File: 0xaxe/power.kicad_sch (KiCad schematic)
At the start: 24 parts, among them Q1 BSS138, Q2 TPH1R712MD,L1Q, Q3 TPH1R712MD,L1Q, Q5 TPH1R712MD,L1Q, U2 1117-3.3, U2 74LVC1G175, U3 AP3211

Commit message: rev1.2
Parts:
- added C218, C225: 1µ, Capacitor_SMD:C_0805_2012Metric, symbol Device:C
- added U113: NCP718xSN500, Package_TO_SOT_SMD:SOT-23-5, symbol Regulator_Linear:NCP718xSN500
- R24: value 84.5k -> 49.9k; Distributor (none) -> D; Manufacturer (none) -> RC0805FR-0749K9L; OrderNr (none) -> 311-49.9KCRCT-ND
- R25: value 16.3k -> 7.15k; Distributor (none) -> D; Manufacturer (none) -> RMCF0805FT7K15; OrderNr (none) -> RMCF0805FT7K15CT-ND
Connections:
- net +5V: now also C218.1, U113.5 (OUT); no longer C9.1, JP1.2 (B), U2.3 (VI)
- net GND: now also C218.2, C225.2, U113.2 (GND)
- new net +6.5V: C225.1, C9.1, JP1.2 (B), U113.1 (IN), U113.3 (EN), U2.3 (VI)
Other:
- moved on the sheet: C15, C2, C24, C4, C9, D9, JP1, JP2, L1, Q1, Q2, Q3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

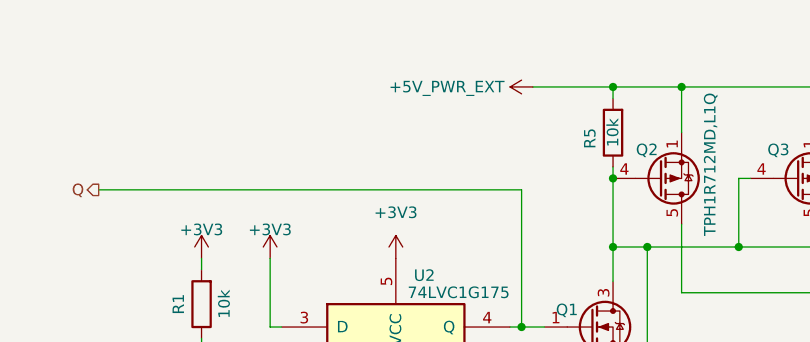
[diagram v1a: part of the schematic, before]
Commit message: Add F2 Fuse for 5V external supply
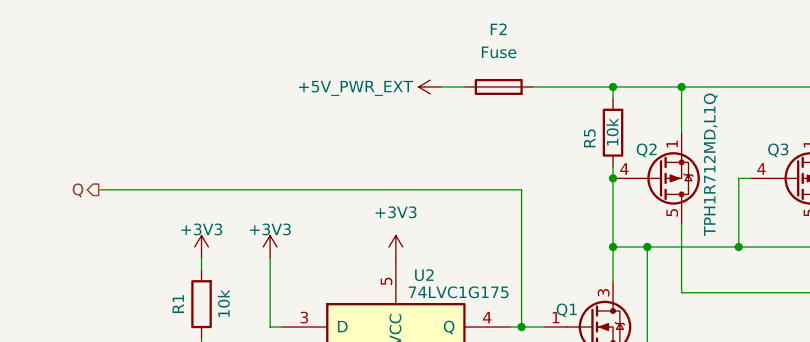
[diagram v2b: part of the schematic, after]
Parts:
- added F2: Fuse, Fuse:Fuseholder_Blade_Mini_Keystone_3568, symbol Device:Fuse
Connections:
- net +5V_PWR_EXT: now also F2.1; no longer Q2.1 (S), Q2.2 (S), Q2.3 (S), Q3.1 (S), Q3.2 (S), Q3.3 (S), Q5.1 (S), Q5.2 (S), Q5.3 (S), R5.2
- new net: F2.2, Q2.1 (S), Q2.2 (S), Q2.3 (S), Q3.1 (S), Q3.2 (S), Q3.3 (S), Q5.1 (S), Q5.2 (S), Q5.3 (S), R5.2
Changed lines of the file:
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@@
 	(wire
 		(pts
+			(xy 124.46 21.59) (xy 127 21.59)
+		)
+		(stroke
+			(width 0)
+			(type default)
+		)
+	)
+	(wire
+		(pts
 			(xy 176.53 115.57) (xy 176.53 127)
 		)
@@
 	)
 	(symbol
+		(lib_id "Device:Fuse")
+		(at 130.81 21.59 90)
+		(unit 1)
+		(exclude_from_sim no)
+		(in_bom yes)
+		(on_board yes)
+		(dnp no)
+		(fields_autoplaced yes)
+		(property "Reference" "F2"
+			(at 130.81 15.24 90)
+			(effects
+				(font
+					(size 1.27 1.27)
+				)
+			)
+		)
+		(property "Value" "Fuse"
+			(at 130.81 17.78 90)
+			(effects
+				(font
+					(size 1.27 1.27)
+				)
+			)
+		)
+		(property "Footprint" "Fuse:Fuseholder_Blade_Mini_Keystone_3568"
+			(at 130.81 23.368 90)
+			(effects
+				(font
+					(size 1.27 1.27)
+				)
+				(hide yes)
+			)
+		)
+		(property "Datasheet" "~"
+			(at 130.81 21.59 0)
+			(effects
+				(font
+					(size 1.27 1.27)
+				)
+				(hide yes)
+			)
+		)
+		(property "Description" "Fuse"
+			(at 130.81 21.59 0)
+			(effects
+				(font
+					(size 1.27 1.27)
+				)
+				(hide yes)
+			)
+		)
+		(pin "1"
+		)
+		(pin "2"
+		)
+		(instances
+			(project "0xaxe"
+				(path "/e63e39d7-6ac0-4ffd-8aa3-1841a4541b55/8ec0a9c6-2b78-44ef-a83d-9047d2828409"
+					(reference "F2")
+					(unit 1)
+				)
+			)
+		)
+	)
+	(symbol
 		(lib_id "74xGxx:74LVC1G175")
 		(at 119.38 53.34 0)
@@
 	(symbol
 		(lib_id "mylib7:+5V_PWR_EXT")
-		(at 134.62 21.59 90)
+		(at 124.46 21.59 90)
 		(unit 1)
 		(exclude_from_sim no)
@@
 		(on_board yes)
 		(dnp no)
-		(fields_autoplaced yes)
 		(property "Reference" "#PWR030"
-			(at 138.43 21.59 0)
+			(at 128.27 21.59 0)
 			(effects
 				(font
@@
 		)
 		(property "Value" "+5V_PWR_EXT"
-			(at 131.445 21.59 90)
+			(at 121.285 21.59 90)
 			(effects
 				(font
@@
 		)
 		(property "Footprint" ""
-			(at 134.62 21.59 0)
+			(at 124.46 21.59 0)
 			(effects
 				(font
@@
 		)
 		(property "Datasheet" ""
-			(at 134.62 21.59 0)
+			(at 124.46 21.59 0)
 			(effects
 				(font
@@
 		)
 		(property "Description" ""
-			(at 134.62 21.59 0)
+			(at 124.46 21.59 0)
 			(effects
 				(font

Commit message: General Update
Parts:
- removed F2: Fuse, Fuse:Fuseholder_Blade_Mini_Keystone_3568, symbol Device:Fuse
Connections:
- net +5V_PWR_EXT: now also Q2.1 (S), Q2.2 (S), Q2.3 (S), Q3.1 (S), Q3.2 (S), Q3.3 (S), Q5.1 (S), Q5.2 (S), Q5.3 (S), R5.2
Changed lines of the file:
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@@
-	(wire
-		(pts
-			(xy 143.51 21.59) (xy 134.62 21.59)
-		)
-		(stroke
-			(width 0)
-			(type default)
-		)
-	)
 	(wire
 		(pts
@@
 	(wire
 		(pts
-			(xy 124.46 21.59) (xy 127 21.59)
+			(xy 124.46 21.59) (xy 143.51 21.59)
 		)
 		(stroke
@@
 					(unit 1)
 				)
-			)
-		)
-	)
-	(symbol
-		(lib_id "Device:Fuse")
-		(at 130.81 21.59 90)
-		(unit 1)
-		(exclude_from_sim no)
-		(in_bom yes)
-		(on_board yes)
-		(dnp no)
-		(fields_autoplaced yes)
-		(property "Reference" "F2"
-			(at 130.81 15.24 90)
-			(effects
-				(font
-					(size 1.27 1.27)
-				)
-			)
-		)
-		(property "Value" "Fuse"
-			(at 130.81 17.78 90)
-			(effects
-				(font
-					(size 1.27 1.27)
-				)
-			)
-		)
-		(property "Footprint" "Fuse:Fuseholder_Blade_Mini_Keystone_3568"
-			(at 130.81 23.368 90)
-			(effects
-				(font
-					(size 1.27 1.27)
-				)
-				(hide yes)
-			)
-		)
-		(property "Datasheet" "~"
-			(at 130.81 21.59 0)
-			(effects
-				(font
-					(size 1.27 1.27)
-				)
-				(hide yes)
-			)
-		)
-		(property "Description" "Fuse"
-			(at 130.81 21.59 0)
-			(effects
-				(font
-					(size 1.27 1.27)
-				)
-				(hide yes)
-			)
-		)
-		(pin "1"
-		)
-		(pin "2"
-		)
-		(instances
-			(project "0xaxe"
-				(path "/e63e39d7-6ac0-4ffd-8aa3-1841a4541b55/8ec0a9c6-2b78-44ef-a83d-9047d2828409"
-					(reference "F2")
-					(unit 1)
-				)

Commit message: fixed couple of things
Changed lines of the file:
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@@
 		)
 		(property "Value" "GND"
-			(at 119.38 73.025 0)
+			(at 119.38 72.39 0)
 			(effects
 				(font
@@
 			)
 		)
-		(property "Description" ""
+		(property "Description" "Power symbol creates a global label with name \"GND\" , ground"
 			(at 119.38 67.31 0)
 			(effects
@@
 			)
 		)
-		(property "Description" ""
+		(property "Description" "Power symbol creates a global label with name \"GND\" , ground"
 			(at 143.51 128.27 0)
 			(effects
@@
 		)
 		(property "Value" "GND"
-			(at 143.51 73.025 0)
+			(at 143.51 72.39 0)
 			(effects
 				(font
@@
 			)
 		)
-		(property "Description" ""
+		(property "Description" "Power symbol creates a global label with name \"GND\" , ground"
 			(at 143.51 67.31 0)
 			(effects
@@
 			)
 		)
-		(property "Description" ""
+		(property "Description" "Power symbol creates a global label with name \"GND\" , ground"
 			(at 176.53 128.27 0)
 			(effects
@@
 		)
 		(property "Value" "GND"
-			(at 105.41 73.025 0)
+			(at 105.41 72.39 0)
 			(effects
 				(font
@@
 			)
 		)
-		(property "Description" ""
+		(property "Description" "Power symbol creates a global label with name \"GND\" , ground"
 			(at 105.41 67.31 0)
 			(effects
@@
 			)
 		)
-		(property "Description" ""
+		(property "Description" "Power symbol creates a global label with name \"GND\" , ground"
 			(at 176.53 160.02 0)
 			(effects
@@
 			)
 		)
-		(property "Description" ""
+		(property "Description" "Power symbol creates a global label with name \"GND\" , ground"
 			(at 118.11 128.27 0)
 			(effects
@@
 	)
 	(symbol
+		(lib_name "PWR_FLAG_1")
+		(lib_id "power:PWR_FLAG")
+		(at 166.37 21.59 0)
+		(unit 1)
+		(exclude_from_sim no)
+		(in_bom yes)
+		(on_board yes)
+		(dnp no)
+		(fields_autoplaced yes)
+		(property "Reference" "#FLG05"
+			(at 166.37 19.685 0)
+			(effects
+				(font
+					(size 1.27 1.27)
+				)
+				(hide yes)
+			)
+		)
+		(property "Value" "PWR_FLAG"
+			(at 166.37 16.51 0)
+			(effects
+				(font
+					(size 1.27 1.27)
+				)
+			)
+		)
+		(property "Footprint" ""
+			(at 166.37 21.59 0)
+			(effects
+				(font
+					(size 1.27 1.27)
+				)
+				(hide yes)
+			)
+		)
+		(property "Datasheet" "~"
+			(at 166.37 21.59 0)
+			(effects
+				(font
+					(size 1.27 1.27)
+				)
+				(hide yes)
+			)
+		)
+		(property "Description" "Special symbol for telling ERC where power comes from"
+			(at 166.37 21.59 0)
+			(effects
+				(font
+					(size 1.27 1.27)
+				)
+				(hide yes)
+			)
+		)
+		(pin "1"
+		)
+		(instances
+			(project "0xaxe"
+				(path "/e63e39d7-6ac0-4ffd-8aa3-1841a4541b55/8ec0a9c6-2b78-44ef-a83d-9047d2828409"
+					(reference "#FLG05")
+					(unit 1)
+				)
+			)
+		)
+	)
+	(symbol
 		(lib_id "power:GND")
 		(at 130.81 128.27 0)
@@
 			)
 		)
-		(property "Description" ""
+		(property "Description" "Power symbol creates a global label with name \"GND\" , ground"
 			(at 130.81 128.27 0)
 			(effects
@@
 			)
 		)
-		(property "Description" ""
+		(property "Description" "Power symbol creates a global label with name \"GND\" , ground"
 			(at 166.37 160.02 0)
 			(effects
@@
 		)
 		(property "Value" "GND"
-			(at 147.32 73.025 0)
+			(at 147.32 72.39 0)
 			(effects
 				(font
@@
 			)
 		)
-		(property "Description" ""
+		(property "Description" "Power symbol creates a global label with name \"GND\" , ground"
 			(at 147.32 67.31 0)
 			(effects
@@
 			)
 		)
-		(property "Description" ""
+		(property "Description" "Power symbol creates a global label with name \"GND\" , ground"
 			(at 97.79 128.27 0)
 			(effects
@@
 		)
 		(property "Value" "GND"
-			(at 97.79 73.025 0)
+			(at 97.79 72.39 0)
 			(effects
 				(font
@@
 			)
 		)
-		(property "Description" ""
+		(property "Description" "Power symbol creates a global label with name \"GND\" , ground"
 			(at 97.79 67.31 0)
 			(effects
@@
 			)
 		)
-		(property "Description" ""
+		(property "Description" "Power symbol creates a global label with name \"GND\" , ground"
 			(at 132.08 67.31 0)
 			(effects
@@
 			)
 		)
-		(property "Description" ""
+		(property "Description" "Power symbol creates a global label with name \"GND\" , ground"
 			(at 86.36 128.27 0)
 			(effects
@@
 			)
 		)
-		(property "Description" ""
+		(property "Description" "Power symbol creates a global label with name \"GND\" , ground"
 			(at 187.96 160.02 0)
 			(effects

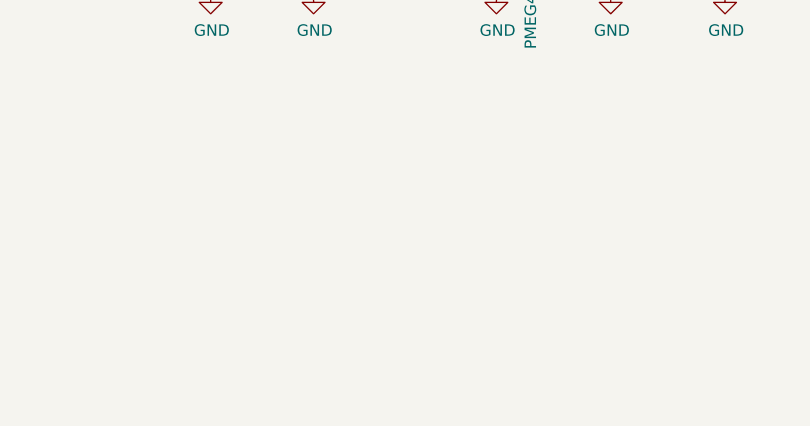
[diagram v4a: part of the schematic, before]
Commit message: fixed level shifter, added optional headers for future extensions
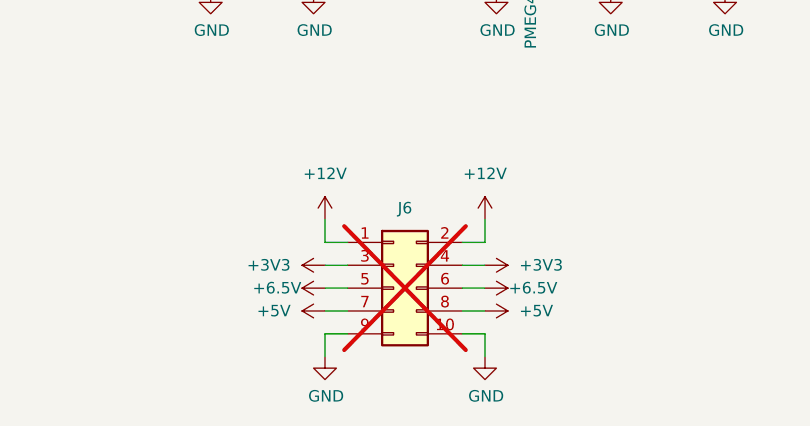
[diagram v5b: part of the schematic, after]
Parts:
- added J6: Conn_02x05_Odd_Even, myfootprints:PinHeader_IDC_2x05_P1.27mm_Vertical_SMD, symbol Connector_Generic:Conn_02x05_Odd_Even
- C9: Distributor (none) -> D; Manufacturer (none) -> CAY16-1002F4LF; OrderNr (none) -> CAY16-1002F4LFCT-ND
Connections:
- net +12V: now also J6.1 (Pin_1), J6.2 (Pin_2)
- net +3V3: now also J6.3 (Pin_3), J6.4 (Pin_4)
- net +5V: now also J6.7 (Pin_7), J6.8 (Pin_8)
- net +6.5V: now also J6.5 (Pin_5), J6.6 (Pin_6)
- net GND: now also J6.10 (Pin_10), J6.9 (Pin_9)

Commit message: fixed BOM
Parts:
- C9: Distributor D -> (none); Manufacturer CAY16-1002F4LF -> (none); OrderNr CAY16-1002F4LFCT-ND -> (none)
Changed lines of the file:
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@@
 			)
 		)
-		(property "Distributor" "D"
+		(property "Distributor" ""
 			(at 166.37 118.11 0)
 			(effects
@@
 			)
 		)
-		(property "Manufacturer" "CAY16-1002F4LF"
+		(property "Manufacturer" ""
 			(at 166.37 118.11 0)
 			(effects
@@
 			)
 		)
-		(property "OrderNr" "CAY16-1002F4LFCT-ND"
+		(property "OrderNr" ""
 			(at 166.37 118.11 0)
 			(effects
@@
 			)
 		)
-		(property "Distributor" "D"
+		(property "Distributor" ""
 			(at 86.36 115.57 0)
 			(effects
@@
 			)
 		)
-		(property "Manufacturer" "CAY16-1002F4LF"
+		(property "Manufacturer" ""
 			(at 86.36 115.57 0)
 			(effects
@@
 			)
 		)
-		(property "OrderNr" "CAY16-1002F4LFCT-ND"
+		(property "OrderNr" ""
 			(at 86.36 115.57 0)
 			(effects

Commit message: fixed bom
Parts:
- JP1, JP2, TP2: now left out of the parts list
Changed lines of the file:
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@@
 		(unit 1)
 		(exclude_from_sim no)
-		(in_bom yes)
+		(in_bom no)
 		(on_board yes)
 		(dnp no)
@@
 		(unit 1)
 		(exclude_from_sim no)
-		(in_bom yes)
+		(in_bom no)
 		(on_board yes)
 		(dnp no)
@@
 		(unit 1)
 		(exclude_from_sim no)
-		(in_bom yes)
-		(on_board yes)
-		(dnp no)
+		(in_bom no)
+		(on_board yes)
+		(dnp no)
